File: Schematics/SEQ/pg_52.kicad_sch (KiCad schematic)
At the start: 16 parts, among them U5301 F374, U5302 F374, U5303 F251, U5304 F251, U5305 F04, U5306 F374, U5307 F04, U5308 F00, U5309 F00, U5310 F00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

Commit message: Fix 0/8 typo
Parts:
- removed GB34, GB35, GB36, GB38: GB, symbol r1000:GB
- removed U5301, U5302, U5306: F374, symbol r1000:F374
- removed U5303, U5304: F251, symbol r1000:F251
- removed U5305, U5307: F04, symbol r1000:F04
- removed U5308, U5309, U5310: F00, symbol r1000:F00
- removed U5311, U5312: F85, symbol r1000:F85
- added U (x3): (no value), symbol r1000:F374
- added U (x2): (no value), symbol r1000:F251
- added U (x2): (no value), symbol r1000:F04
- added U (x3): (no value), symbol r1000:F00
- added U (x4): (no value), symbol r1000:GB
- added U (x2): (no value), symbol r1000:F85
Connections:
- net BRK_MSK.CLK~: now also U.11 (CLK), U.11 (CLK)
- net CSA_FREE.DEC0: now also U.12 (A2)
- net CSA_FREE.DEC1: now also U.10 (A3)
- net CSA_VALID.DEC0: now also U.13 (A1)
- net CSA_VALID.DEC1: now also U.12 (A2)
- net CSA_VALID.DEC2: now also U.10 (A3)
- net CUR_CLASS0: now also U.1 (D0), U.7 (OE)
- net CUR_CLASS1: now also U.11 (S2), U.11 (S2)
- net CUR_CLASS2: now also U.10 (S1), U.10 (S1)
- net CUR_CLASS3: now also U.9 (S0), U.9 (S0)
- net DISP~0: now also U.1 (D0)
- net IBUFF_EMPTY: now also U.1 (D0)
- net IBUFF_FILL~.DEC: now also U.2 (D1)
- net LEX_VLD.COND~: now also U.2 (D1)
- net M_BRK_CLASS~: now also U.6 (Y~), U.6 (Y~)
- net M_IBUFF_MT~: now also U.3 (Q)
- net M_OVERFLOW~: now also U.5 (A>B)
- net M_RES_REF~: now also U.3 (Q)
- net M_TOS_INVLD~: now also U.3 (Q)
- net M_UNDERFLOW~: now also U.7 (A<B)
- net N_IN_CSA.CLK~: now also U.11 (CLK)
- net N_IN_CSA0: now also U.2 (Q0)
- net N_IN_CSA1: now also U.5 (Q1)
- net N_IN_CSA2: now also U.6 (Q2)
- net N_IN_CSA3: now also U.9 (Q3)
- net PD: now also U.1 (OE), U.1 (OE), U.1 (OE), U.15 (A0), U.2 (E<), U.3 (D0), U.3 (E=), U.3 (E=), U.4 (E>)
- net PU: now also U.13 (A1), U.15 (A0), U.2 (E<), U.4 (E>)
- net Q.CSA_NVE0: now also U.1, U.1 (B0), U.1 (B0), U.3 (D0)
- net Q.CSA_NVE1: now also U.1, U.14 (B1), U.14 (B1), U.4 (D1)
- net Q.CSA_NVE2: now also U.1, U.11 (B2), U.11 (B2), U.7 (D2)
- net Q.CSA_NVE3: now also U.1, U.8 (D3), U.9 (B3), U.9 (B3)
- net TOS_VLD.COND~: now also U.2 (D1)
- net USES_TOS.DEC: now also U.1 (D0)
- net VAL~33: now also U.4 (D1)
- net VAL~34: now also U.7 (D2)
- net VAL~35: now also U.8 (D3)
- net VAL~36: now also U.13 (D4)
- net VAL~37: now also U.14 (D5)
- net VAL~38: now also U.17 (D6)
- net VAL~39: now also U.18 (D7)
- net VAL~40: now also U.3 (D0)
- net VAL~41: now also U.4 (D1)
- net VAL~42: now also U.7 (D2)
- net VAL~43: now also U.8 (D3)
- net VAL~44: now also U.13 (D4)
- net VAL~45: now also U.14 (D5)
- net VAL~46: now also U.17 (D6)
- net VAL~47: now also U.18 (D7)
- new net: U.12 (Q4), U.15 (E) (x2)
- new net: U.14 (F), U.15 (Q5) (x2)
- new net: U.13 (G), U.16 (Q6) (x2)
- new net: U.12 (H), U.19 (Q7) (x2)
- new net: U.2 (Q0), U.4 (A) (x2)
- new net: U.3 (B), U.5 (Q1) (x2)
- new net: U.2 (C), U.6 (Q2) (x2)
- new net: U.1 (D), U.9 (Q3) (x2)
- new net: U.1 (D0), U.2 (Q)
- new net: U.2 (Q), U.7 (OE)

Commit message: Tested until 5.8 seconds (rm029)
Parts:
- removed U (x2): (no value), symbol r1000:F374
- removed U (x2): (no value), symbol r1000:F251
- removed U: (no value), symbol r1000:F04
- added U: XREG16, symbol r1000:XREG16
- added U: XMUX16_1, symbol r1000:XMUX16_1
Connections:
- net BRK_MSK.CLK~: now also U.1 (CLK)
- net CUR_CLASS0: now also U.1 (S0)
- net CUR_CLASS1: now also U.4 (S3)
- net CUR_CLASS2: now also U.3 (S2)
- net CUR_CLASS3: now also U.2 (S1)
- net M_BRK_CLASS~: now also U.6 (Y~)
- net PD: now also U.3 (OE), U.6 (D0)
- net VAL~33: now also U.8 (D1)
- net VAL~34: now also U.10 (D2)
- net VAL~35: now also U.12 (D3)
- net VAL~36: now also U.14 (D4)
- net VAL~37: now also U.16 (D5)
- net VAL~38: now also U.18 (D6)
- net VAL~39: now also U.20 (D7)
- net VAL~40: now also U.22 (D8)
- net VAL~41: now also U.24 (D9)
- net VAL~42: now also U.26 (D10)
- net VAL~43: now also U.28 (D11)
- net VAL~44: now also U.30 (D12)
- net VAL~45: now also U.32 (D13)
- net VAL~46: now also U.34 (D14)
- net VAL~47: now also U.36 (D15)
- new net: U.11 (Q2), U.7 (I2)
- new net: U.13 (Q3), U.8 (I3)
- new net: U.15 (Q4), U.9 (I4)
- new net: U.10 (I5), U.17 (Q5)
- new net: U.11 (I6), U.19 (Q6)
- new net: U.12 (I7), U.21 (Q7)
- new net: U.13 (I8), U.23 (Q8)
- new net: U.14 (I9), U.25 (Q9)
- new net: U.15 (I10), U.27 (Q10)
- new net: U.16 (I11), U.29 (Q11)
- new net: U.17 (I12), U.31 (Q12)
- new net: U.18 (I13), U.33 (Q13)
- new net: U.19 (I14), U.35 (Q14)
- new net: U.20 (I15), U.37 (Q15)
- new net: U.5 (Y), U.7 (Q0)
- new net: U.6 (Y~), U.9 (Q1)

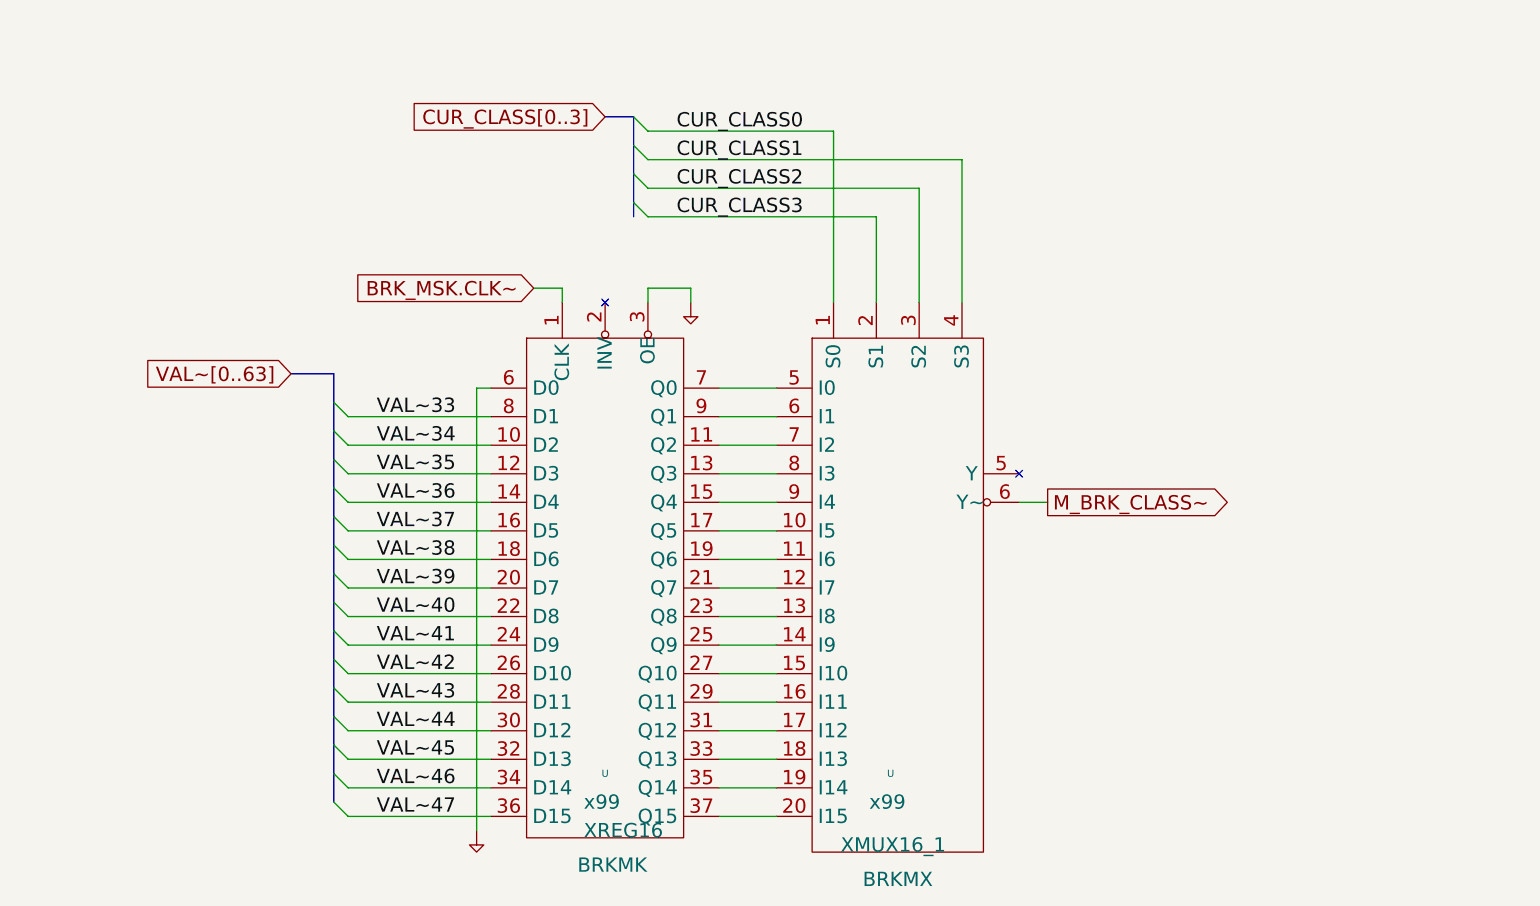
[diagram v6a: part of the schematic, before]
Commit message: Tested to 6.3 seconds (rm045)
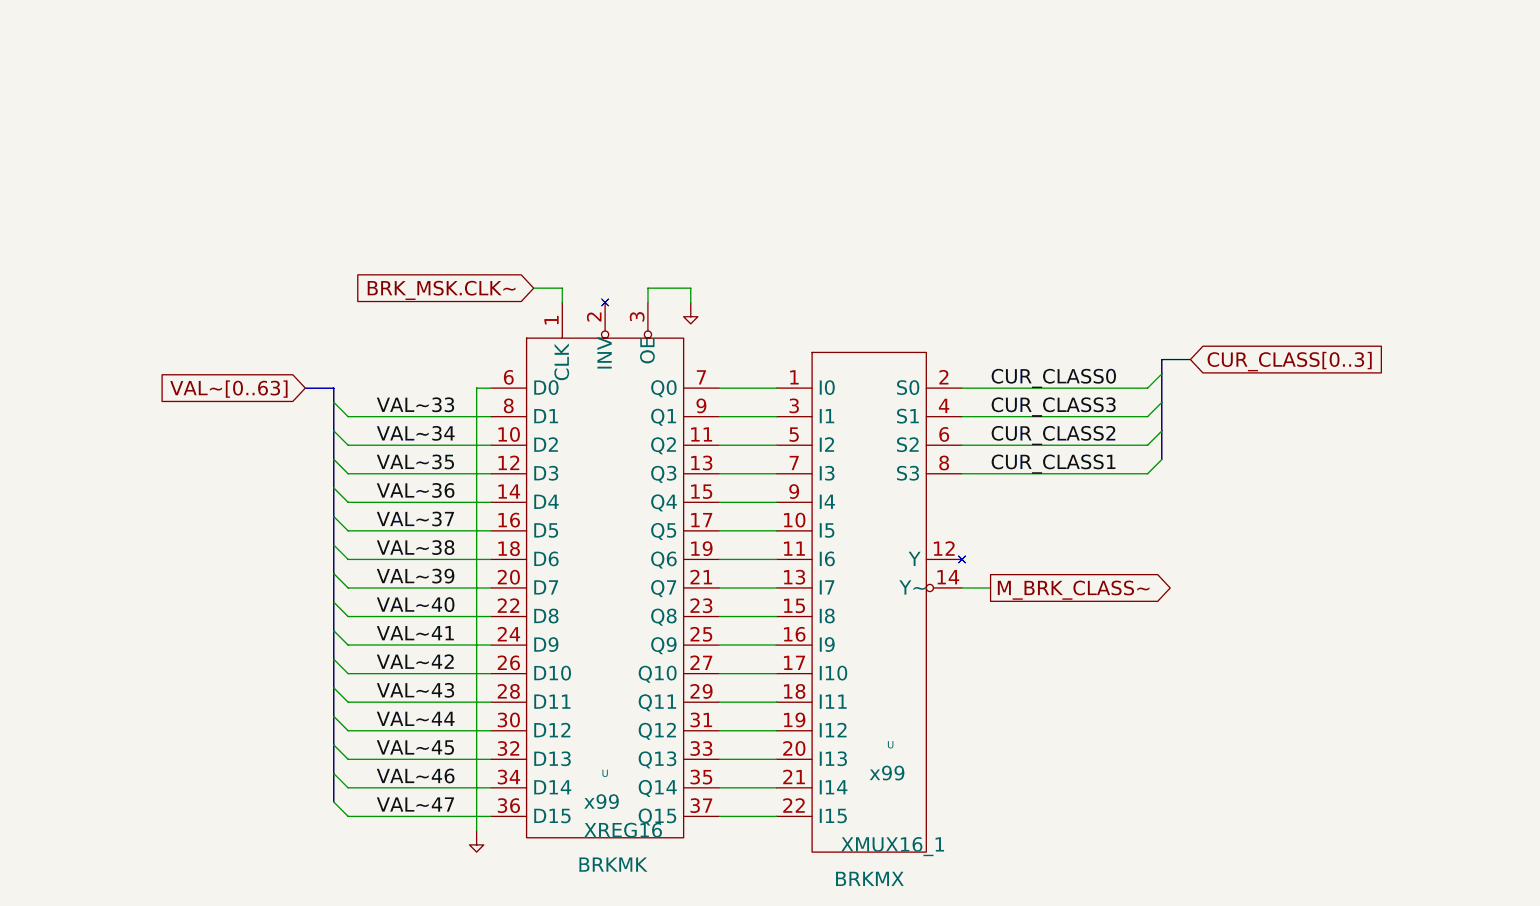
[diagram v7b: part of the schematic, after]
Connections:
- net CUR_CLASS0: now also U.2 (S0); no longer U.1 (S0)
- net CUR_CLASS1: now also U.8 (S3); no longer U.4 (S3)
- net CUR_CLASS2: now also U.6 (S2); no longer U.3 (S2)
- net CUR_CLASS3: now also U.4 (S1); no longer U.2 (S1)
- net M_BRK_CLASS~: now also U.14 (Y~); no longer U.6 (Y~)
- net at U.11 (Q2): now also U.5 (I2); no longer U.7 (I2)
- net at U.13 (Q3): now also U.7 (I3); no longer U.8 (I3)
- net at U.21 (Q7): now also U.13 (I7); no longer U.12 (I7)
- net at U.23 (Q8): now also U.15 (I8); no longer U.13 (I8)
- net at U.25 (Q9): now also U.16 (I9); no longer U.14 (I9)
- net at U.27 (Q10): now also U.17 (I10); no longer U.15 (I10)
- net at U.29 (Q11): now also U.18 (I11); no longer U.16 (I11)
- net at U.31 (Q12): now also U.19 (I12); no longer U.17 (I12)
- net at U.33 (Q13): now also U.20 (I13); no longer U.18 (I13)
- net at U.35 (Q14): now also U.21 (I14); no longer U.19 (I14)
- net at U.37 (Q15): now also U.22 (I15); no longer U.20 (I15)
- net at U.7 (Q0): now also U.1 (I0); no longer U.5 (Y)
- net at U.9 (Q1): now also U.3 (I1); no longer U.6 (Y~)
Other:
- moved on the sheet: U
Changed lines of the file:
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@@
   (no_connect (at 238.76 48.26))
   (no_connect (at 109.22 175.26))
-  (no_connect (at 388.62 264.16))
+  (no_connect (at 378.46 279.4))
   (no_connect (at 238.76 43.18))
   (no_connect (at 109.22 185.42))
@@
     (stroke (width 0) (type default))
   )
-  (bus_entry (at 320.04 215.9) (size 2.54 2.54)
+  (bus_entry (at 414.02 261.62) (size -2.54 2.54)
     (stroke (width 0) (type default))
   )
@@
     (stroke (width 0) (type default))
   )
-  (bus_entry (at 320.04 210.82) (size 2.54 2.54)
+  (bus_entry (at 414.02 256.54) (size -2.54 2.54)
     (stroke (width 0) (type default))
   )
@@
     (stroke (width 0) (type default))
   )
-  (bus_entry (at 320.04 205.74) (size 2.54 2.54)
+  (bus_entry (at 414.02 251.46) (size -2.54 2.54)
     (stroke (width 0) (type default))
   )
@@
     (stroke (width 0) (type default))
   )
-  (bus_entry (at 320.04 200.66) (size 2.54 2.54)
+  (bus_entry (at 414.02 246.38) (size -2.54 2.54)
     (stroke (width 0) (type default))
   )
@@
     (stroke (width 0) (type default))
   )
-  (wire (pts (xy 322.58 213.36) (xy 370.84 213.36))
-    (stroke (width 0) (type default))
-  )
   (wire (pts (xy 208.28 114.3) (xy 76.2 114.3))
     (stroke (width 0) (type default))
@@
     (stroke (width 0) (type default))
   )
-  (wire (pts (xy 322.58 208.28) (xy 378.46 208.28))
-    (stroke (width 0) (type default))
-  )
   (wire (pts (xy 58.42 58.42) (xy 63.5 58.42))
     (stroke (width 0) (type default))
@@
     (stroke (width 0) (type default))
   )
-  (wire (pts (xy 355.6 203.2) (xy 355.6 233.68))
-    (stroke (width 0) (type default))
-  )
   (wire (pts (xy 121.92 134.62) (xy 121.92 132.08))
     (stroke (width 0) (type default))
@@
     (stroke (width 0) (type default))
   )
-  (bus (pts (xy 266.7 246.38) (xy 266.7 251.46))
-    (stroke (width 0) (type default))
-  )
-  (wire (pts (xy 363.22 218.44) (xy 363.22 233.68))
+  (bus (pts (xy 266.7 248.92) (xy 266.7 251.46))
     (stroke (width 0) (type default))
   )
@@
     (stroke (width 0) (type default))
   )
-  (wire (pts (xy 363.22 218.44) (xy 322.58 218.44))
-    (stroke (width 0) (type default))
-  )
   (wire (pts (xy 208.28 22.86) (xy 203.2 22.86))
     (stroke (width 0) (type default))
@@
     (stroke (width 0) (type default))
   )
-  (bus (pts (xy 320.04 210.82) (xy 320.04 215.9))
+  (bus (pts (xy 414.02 256.54) (xy 414.02 261.62))
     (stroke (width 0) (type default))
   )
@@
     (stroke (width 0) (type default))
   )
-  (bus (pts (xy 320.04 215.9) (xy 320.04 218.44))
-    (stroke (width 0) (type default))
-  )
   (wire (pts (xy 63.5 165.1) (xy 109.22 165.1))
     (stroke (width 0) (type default))
@@
     (stroke (width 0) (type default))
   )
-  (wire (pts (xy 388.62 269.24) (xy 393.7 269.24))
+  (wire (pts (xy 378.46 284.48) (xy 383.54 284.48))
     (stroke (width 0) (type default))
   )
@@
     (stroke (width 0) (type default))
   )
-  (wire (pts (xy 378.46 208.28) (xy 378.46 233.68))
-    (stroke (width 0) (type default))
-  )
   (wire (pts (xy 63.5 58.42) (xy 66.04 58.42))
     (stroke (width 0) (type default))
@@
     (stroke (width 0) (type default))
   )
-  (bus (pts (xy 314.96 200.66) (xy 320.04 200.66))
+  (bus (pts (xy 419.1 243.84) (xy 414.02 243.84))
     (stroke (width 0) (type default))
   )
@@
     (stroke (width 0) (type default))
   )
+  (wire (pts (xy 378.46 259.08) (xy 411.48 259.08))
+    (stroke (width 0) (type default))
+  )
   (wire (pts (xy 142.24 154.94) (xy 187.96 154.94))
     (stroke (width 0) (type default))
@@
     (stroke (width 0) (type default))
   )
+  (bus (pts (xy 414.02 246.38) (xy 414.02 251.46))
+    (stroke (width 0) (type default))
+  )
   (wire (pts (xy 269.24 259.08) (xy 294.64 259.08))
     (stroke (width 0) (type default))
@@
     (stroke (width 0) (type default))
   )
+  (wire (pts (xy 378.46 248.92) (xy 411.48 248.92))
+    (stroke (width 0) (type default))
+  )
+  (wire (pts (xy 378.46 254) (xy 411.48 254))
+    (stroke (width 0) (type default))
+  )
   (bus (pts (xy 266.7 292.1) (xy 266.7 297.18))
     (stroke (width 0) (type default))
@@
     (stroke (width 0) (type default))
   )
-  (bus (pts (xy 320.04 205.74) (xy 320.04 210.82))
+  (bus (pts (xy 414.02 251.46) (xy 414.02 256.54))
     (stroke (width 0) (type default))
   )
@@
     (stroke (width 0) (type default))
   )
-  (wire (pts (xy 355.6 203.2) (xy 322.58 203.2))
-    (stroke (width 0) (type default))
-  )
   (bus (pts (xy 266.7 251.46) (xy 266.7 256.54))
     (stroke (width 0) (type default))
@@
     (stroke (width 0) (type default))
   )
-  (bus (pts (xy 259.08 246.38) (xy 266.7 246.38))
+  (wire (pts (xy 378.46 264.16) (xy 411.48 264.16))
+    (stroke (width 0) (type default))
+  )
+  (bus (pts (xy 261.62 248.92) (xy 266.7 248.92))
     (stroke (width 0) (type default))
   )
@@
     (stroke (width 0) (type default))
   )
-  (bus (pts (xy 320.04 200.66) (xy 320.04 205.74))
+  (bus (pts (xy 414.02 243.84) (xy 414.02 246.38))
     (stroke (width 0) (type default))
   )
@@
     (stroke (width 0) (type default))
   )
-  (wire (pts (xy 370.84 213.36) (xy 370.84 233.68))
-    (stroke (width 0) (type default))
-  )
   (wire (pts (xy 53.34 132.08) (xy 121.92 132.08))
     (stroke (width 0) (type default))
@@
     (effects (font (size 2.54 2.54)) (justify left bottom))
   )
-  (label "CUR_CLASS2" (at 327.66 213.36 0) (fields_autoplaced)
+  (label "CUR_CLASS2" (at 383.54 259.08 0) (fields_autoplaced)
     (effects (font (size 2.54 2.54)) (justify left bottom))
   )
@@
     (effects (font (size 2.54 2.54)) (justify left bottom))
   )
-  (label "CUR_CLASS3" (at 327.66 218.44 0) (fields_autoplaced)
+  (label "CUR_CLASS3" (at 383.54 254 0) (fields_autoplaced)
     (effects (font (size 2.54 2.54)) (justify left bottom))
   )
@@
     (effects (font (size 2.54 2.54)) (justify left bottom))
   )
-  (label "CUR_CLASS1" (at 327.66 208.28 0) (fields_autoplaced)
+  (label "CUR_CLASS1" (at 383.54 264.16 0) (fields_autoplaced)
     (effects (font (size 2.54 2.54)) (justify left bottom))
   )
@@
     (effects (font (size 2.54 2.54)) (justify left bottom))
   )
-  (label "CUR_CLASS0" (at 327.66 203.2 0) (fields_autoplaced)
+  (label "CUR_CLASS0" (at 383.54 248.92 0) (fields_autoplaced)
     (effects (font (size 2.54 2.54)) (justify left bottom))
   )
@@
     )
   )
-  (global_label "CUR_CLASS[0..3]" (shape input) (at 314.96 200.66 180) (fields_autoplaced)
-    (effects (font (size 2.54 2.54)) (justify right))
-    (property "Intersheet References" "${INTERSHEET_REFS}" (id 0) (at 278.2026 200.5013 0)
-      (effects (font (size 1.905 1.905)) (justify right))
+  (global_label "CUR_CLASS[0..3]" (shape input) (at 419.1 243.84 0) (fields_autoplaced)
+    (effects (font (size 2.54 2.54)) (justify left))
+    (property "Intersheet References" "${INTERSHEET_REFS}" (id 0) (at 455.8574 243.6813 0)
+      (effects (font (size 1.905 1.905)) (justify left))
     )
   )
@@
     )
   )
-  (global_label "M_BRK_CLASS~" (shape output) (at 393.7 269.24 0) (fields_autoplaced)
+  (global_label "M_BRK_CLASS~" (shape output) (at 383.54 284.48 0) (fields_autoplaced)
     (effects (font (size 2.54 2.54)) (justify left))
-    (property "Intersheet References" "${INTERSHEET_REFS}" (id 0) (at 426.345 269.0813 0)
+    (property "Intersheet References" "${INTERSHEET_REFS}" (id 0) (at 416.185 284.3213 0)
       (effects (font (size 1.905 1.905)) (justify left))
     )
@@
     )
   )
-  (global_label "VAL~[0..63]" (shape input) (at 259.08 246.38 180) (fields_autoplaced)
-    (effects (font (size 2.54 2.54)) (justify right))
-    (property "Intersheet References" "${INTERSHEET_REFS}" (id 0) (at 232.1093 246.38 0)
+  (global_label "VAL~[0..63]" (shape input) (at 261.62 248.92 180) (fields_autoplaced)
+    (effects (font (size 2.54 2.54)) (justify right))
+    (property "Intersheet References" "${INTERSHEET_REFS}" (id 0) (at 234.6493 248.92 0)
       (effects (font (size 1.905 1.905)) (justify right))
     )
@@
     (pin "1")
   )
-  (symbol (lib_id "r1000:XMUX16_1") (at 363.22 322.58 0) (unit 1)
+  (symbol (lib_id "r1000:XMUX16_1") (at 363.22 317.5 0) (unit 1)
     (in_bom yes) (on_board yes)
     (default_instance (reference "U") (unit 1) (value "XMUX16_1") (footprint ""))
-    (property "Reference" "U" (id 0) (at 365.76 317.5 0)
+    (property "Reference" "U" (id 0) (at 365.76 312.42 0)
       (effects (font (size 1.27 1.27)))
     )
@@
       (effects (font (size 2.54 2.54)) (justify left))
     )
-    (property "Footprint" "" (id 2) (at 364.49 323.85 0)
-      (effects (font (size 1.27 1.27)) hide)
-    )
-    (property "Datasheet" "" (id 3) (at 364.49 323.85 0)
-      (effects (font (size 1.27 1.27)) hide)
-    )
-    (property "Location" "x99" (id 4) (at 361.95 322.58 0)
+    (property "Footprint" "" (id 2) (at 364.49 318.77 0)
+      (effects (font (size 1.27 1.27)) hide)
+    )
+    (property "Datasheet" "" (id 3) (at 364.49 318.77 0)
+      (effects (font (size 1.27 1.27)) hide)
+    )
+    (property "Location" "x99" (id 4) (at 361.95 317.5 0)
       (effects (font (size 2.54 2.54)) (justify left))
     )
-    (property "Name" "BRKMX" (id 5) (at 367.03 337.82 0)
+    (property "Name" "BRKMX" (id 5) (at 361.95 337.82 0)
       (effects (font (size 2.54 2.54)) (justify bottom))
     )
@@
     (pin "2")
     (pin "20")
+    (pin "21")
+    (pin "22")
     (pin "3")
     (pin "4")
     (pin "5")
-    (pin "5")
-    (pin "6")
     (pin "6")
     (pin "7")

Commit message: New kicad + MEM32 polish
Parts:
- GB34, GB35, GB36, GB38: renamed from U; value (none) -> GB
- U5306: renamed from U; value (none) -> F374
- U5307: renamed from U; value (none) -> F04
- U5308, U5309, U5310: renamed from U; value (none) -> F00
- U5311, U5312: renamed from U; value (none) -> F85
- renumbered U to U53, U to U54
